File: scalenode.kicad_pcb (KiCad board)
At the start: 4 copper layers, 155.5 x 40 mm, 135 parts, among them IC1 TPS2378DDA, J1 B2B-XH-A_LF__SN_, J10 LSHM-130-01-L-RH-A-S-K-TR, J3 1-2199230-6, J4 1140084168, J5 0473460001, J6 SS-74800-144, J7 DF40HC(3.0)-100DS-0.4v, J8 DF40HC(3.0)-100DS-0.4v, M1 compute-module-4-1.5mm, Q6 BSS138-7-F, U1 TS3USB30EDGSR, U2 TPS62823DLCT, U5 TS3USB30EDGSR, U6 FT234XD-R

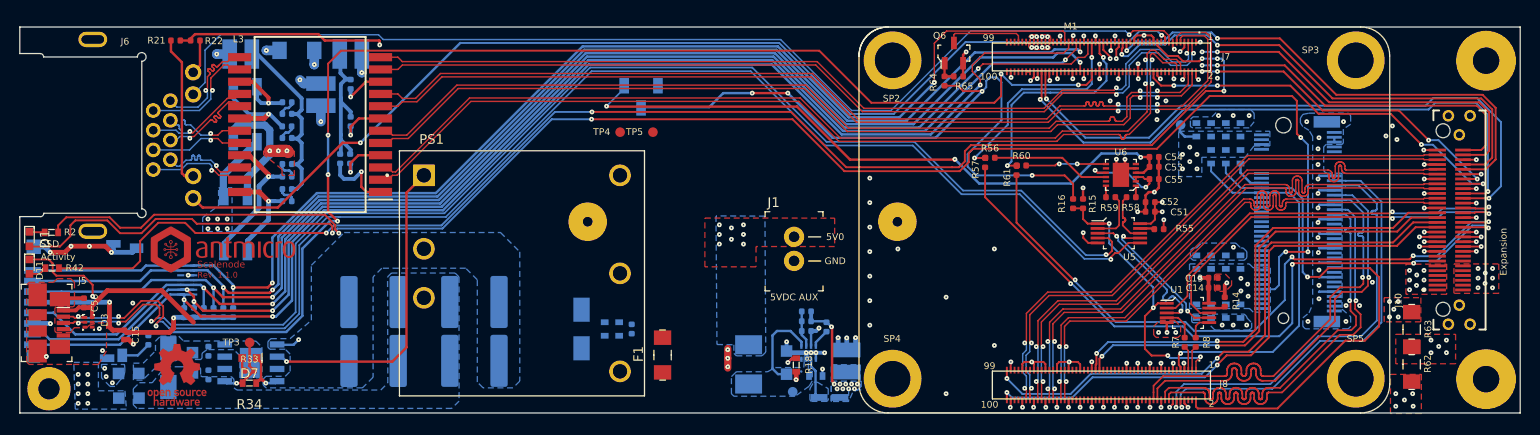
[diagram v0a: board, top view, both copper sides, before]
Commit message: Initial connection of all nets
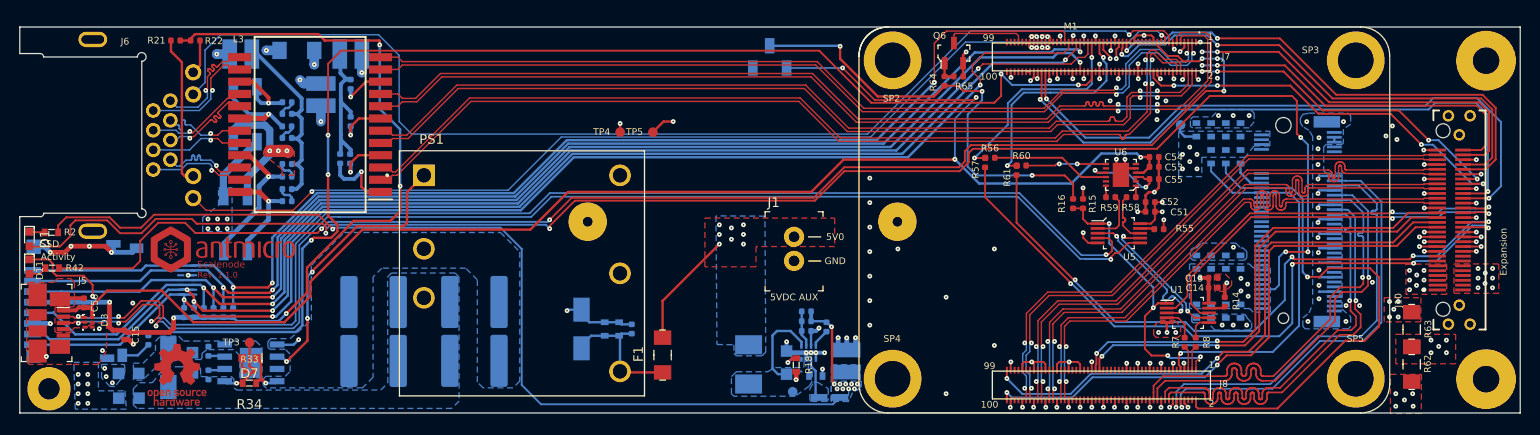
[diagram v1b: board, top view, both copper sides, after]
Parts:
- moved S1 14.0 mm to (132.8, 59.7), turned to 180 degrees
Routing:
- net /Interfaces/VBus_Slave: track 83.5 -> 157.4 mm, vias 3 -> 4
- net 3V3_SSD: track 44.3 -> 111.9 mm
- net 3V3_RPi: track 74.3 -> 116.1 mm, vias 16 -> 18
- net PROG_MODE: track 70.7 -> 47.3 mm, vias 4 -> 3
- net VCC5V0: track 0.00 -> 14.7 mm, vias 24 -> 25
- net Net-(C35-Pad1): track 0.00 -> 14.2 mm
- net /Interfaces/CONN_USB_P: track 140.5 -> 130.2 mm
- net /Interfaces/CONN_USB_N: track 142.0 -> 133.9 mm
- net ETH_LEDY: track 115.7 -> 109.1 mm
- net GND: track 157.3 -> 163.9 mm, vias 151 -> 150
- net SD_DAT3: track 132.8 -> 126.7 mm
- net SD_DAT2: track 134.1 -> 128.0 mm
- net SD_CMD: track 132.9 -> 126.8 mm
- net SD_DAT0: track 135.1 -> 129.0 mm
- net SD_CLK: track 136.5 -> 130.5 mm
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
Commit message: Shortened board. Adjusted posiitons of components. Routed all signals. Added stitching cap
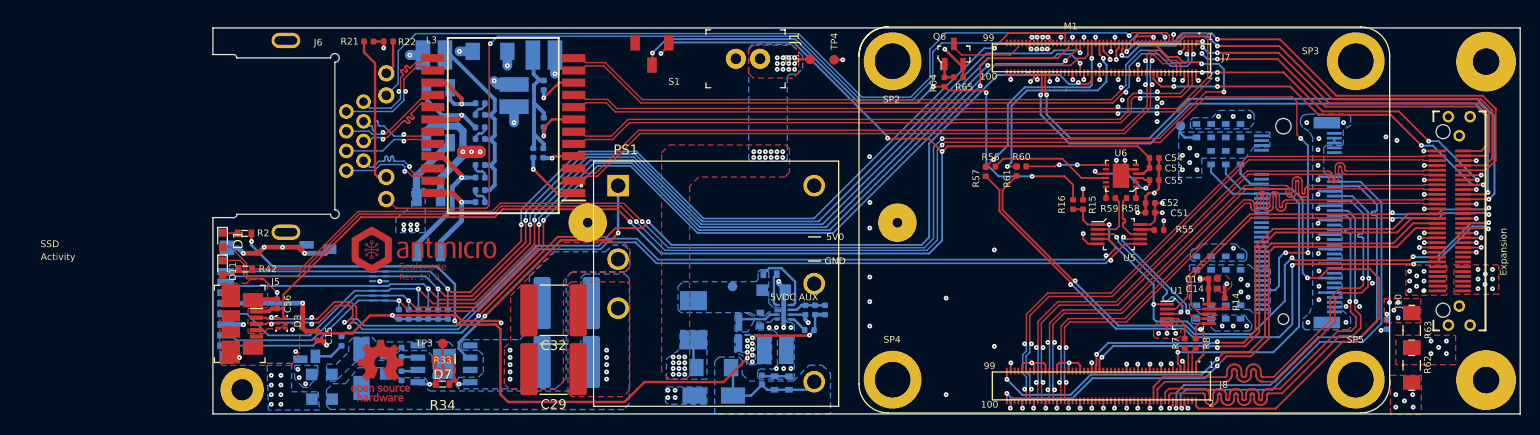
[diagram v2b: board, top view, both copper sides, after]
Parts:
- added C21: C_100n_0402, scalenode-footprints:0402-cap, B.Cu at (196.8, 87.4)
- C29, C32, S1: moved to F.Cu
- F1, R18: moved to B.Cu
- moved TP4 23.4 mm to (139.5, 60.0), turned to -90 degrees
- moved R11 22.3 mm to (97.4, 86.4)
- moved R12 22.3 mm to (98.4, 86.4)
- moved R9 22.3 mm to (95.4, 86.4)
- moved R10 22.3 mm to (96.4, 86.4)
- moved R13 22.3 mm to (99.5, 86.4)
- moved R5 22.3 mm to (94.4, 86.4)
- moved N3 21.1 mm to (92.5, 92.2)
- moved N1 20.8 mm to (97.4, 79.8)
- moved PS1 20.2 mm to (127.2, 83.2)
- moved R28 20.0 mm to (109.3, 69.7)
- moved R27 20.0 mm to (108.3, 69.7)
- moved C20 20.0 mm to (93.0, 91.5)
- moved C25 20.0 mm to (109.4, 59.5)
- moved C26 20.0 mm to (111.8, 85.2)
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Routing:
- net 3V3_RPi: track 116.1 -> 63.5 mm, vias 18 -> 16
- net GPIO3: track 132.7 -> 98.2 mm, vias 5 -> 3
- net 3V3_SSD: track 111.9 -> 80.1 mm, vias 25 -> 27
- net /Interfaces/CONN_USB_N: track 133.9 -> 103.5 mm
- net /Interfaces/CONN_USB_P: track 130.2 -> 102.5 mm
- net ETH_LEDG: track 119.5 -> 94.2 mm
- net TRD2_N: track 100.7 -> 75.6 mm
- net TRD1_N: track 93.1 -> 68.4 mm
- net TRD0_P: track 97.0 -> 72.6 mm
- net TRD1_P: track 93.1 -> 69.0 mm
- net TRD0_N: track 97.1 -> 73.3 mm
- net TRD2_P: track 100.7 -> 77.3 mm
- net TRD3_P: track 93.0 -> 72.1 mm
- net TRD3_N: track 92.5 -> 71.6 mm
- net SD_DAT1: track 130.8 -> 110.7 mm
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- added copper zone on F.Cu, net /PoE/VDD_POE_IN
- added copper zone on F.Cu, net GNDD
- added copper zone on B.Cu, net Net-(C35-Pad1)
- removed copper zone on F.Cu, net Net-(D4-Pad2)
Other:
- board size 155.5 x 40 mm -> 135.5 x 40 mm

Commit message: Optimized routes. Added missing 3D models
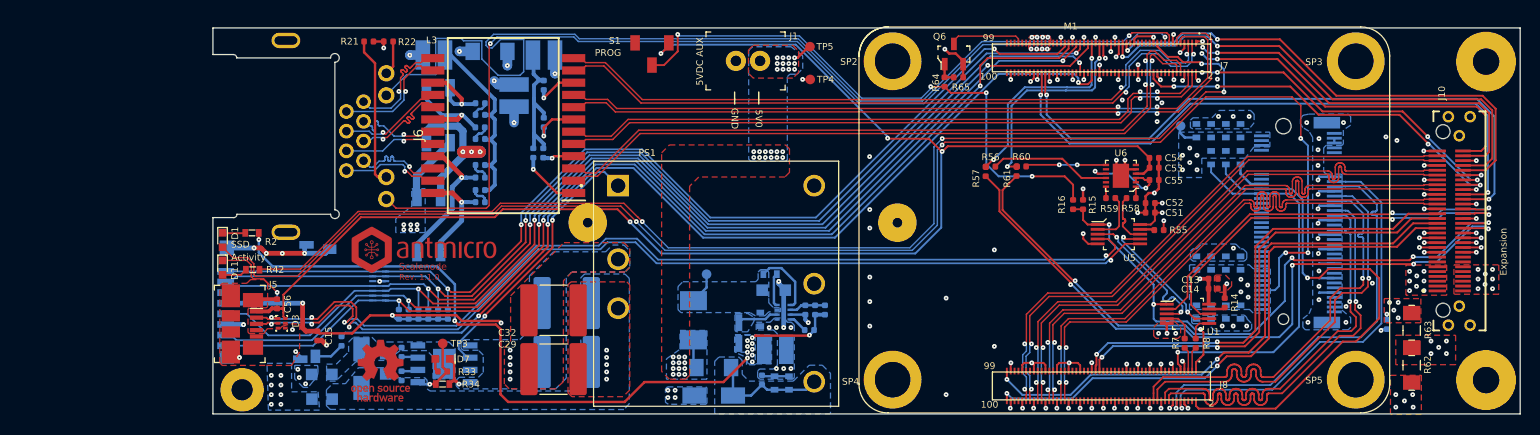
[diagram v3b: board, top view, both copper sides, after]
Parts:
- moved TP4 3.21 mm to (137.0, 62.0)
- moved TP1 2.98 mm to (126.3, 82.2)
- moved TP5 1.31 mm to (137.0, 58.6)
- moved R2 0.77 mm to (79.2, 77.9)
- moved R42 0.77 mm to (79.2, 81.8)
- moved J1 0.22 mm to (131.8, 60.1)
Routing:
- net ETH_LEDG: track 94.2 -> 106.8 mm
- net Net-(C16-Pad1): track 6.96 -> 10.3 mm
- net Net-(J7-Pad21): track 128.3 -> 126.7 mm
- net GND: track 154.0 -> 155.5 mm
- net ETH_LEDY: track 105.6 -> 104.2 mm
- net /Interfaces/VBus_Slave: track 150.4 -> 149.3 mm
- net RPi_RXD: track 22.6 -> 21.7 mm
- net Net-(J6-Pad12): track 3.59 -> 2.71 mm
- net Net-(D1-Pad2): track 154.6 -> 153.8 mm
- net SD_DAT2: track 109.9 -> 109.1 mm
- net Net-(D1-Pad1): track 1.87 -> 2.65 mm
- net Net-(D11-Pad2): track 2.18 -> 2.92 mm
- net SD_DAT1: track 110.7 -> 111.3 mm
- net GPIO26: track 41.4 -> 40.9 mm
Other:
- board text added: "Rev. ${REVISION}"
- board text removed: "Rev. 1.1.0"

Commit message: Corrected footprints. Adjusted position of testpoints. Cleared DRC
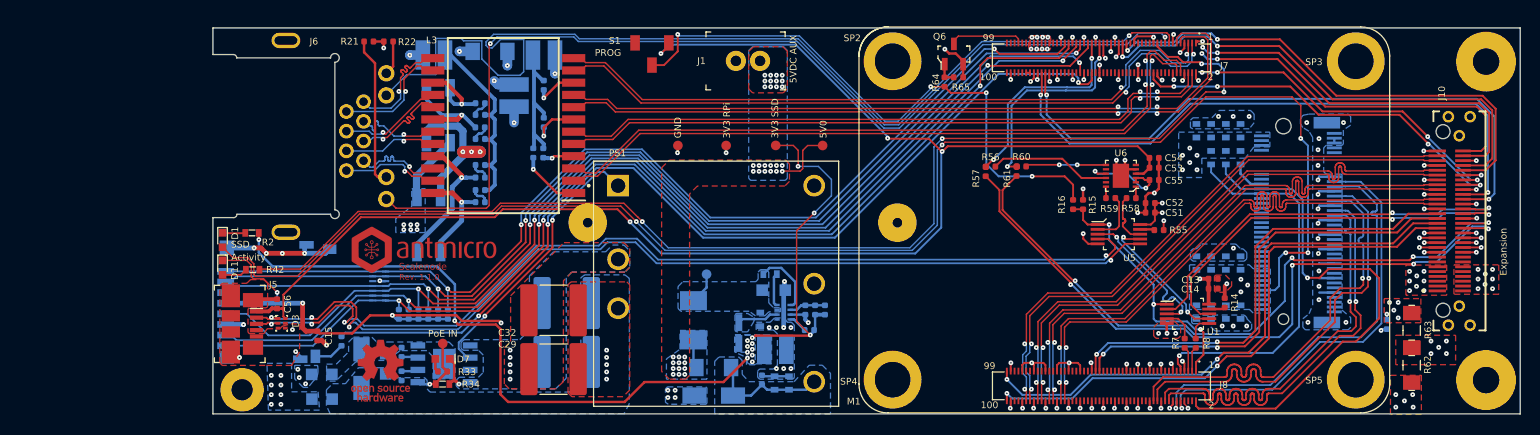
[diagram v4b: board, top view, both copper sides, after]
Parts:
- added TP6: TP_SMD1MM, scalenode-footprints:Testpoint_smd_1mm, F.Cu at (128.3, 68.9)
- TP2: moved to F.Cu
- moved TP2 42.0 mm to (133.5, 68.9), turned to 90 degrees
- moved TP4 15.3 mm to (123.3, 68.9), turned to 0 degrees
- moved TP5 10.3 mm to (138.3, 68.9)
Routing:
- net 3V3_SSD: track 79.9 -> 103.7 mm, vias 27 -> 29
- net VCC5V0: track 5.06 -> 9.39 mm
- net ETH_LEDG: track 106.8 -> 109.7 mm
- net ETH_LEDY: track 104.2 -> 106.3 mm
- net PROG_MODE: track 59.4 -> 61.4 mm
- net Net-(J6-Pad12): track 2.71 -> 3.59 mm
- net 3V3_RPi: track 63.5 -> 64.0 mm, vias 16 -> 17
- net GND: track 155.5 -> 155.2 mm, vias 149 -> 130
- net (no net): vias 1 -> 0
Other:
- board text added: "3V3 RPi"
- board text added: "3V3 SSD"
- board text added: "PoE IN"

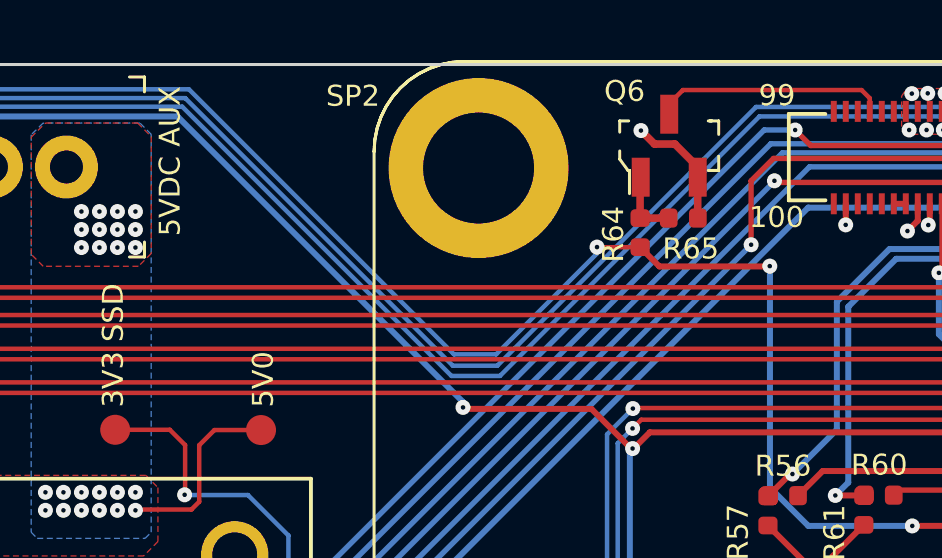
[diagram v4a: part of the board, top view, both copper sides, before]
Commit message: Added stackup table and defined stackup in board settings
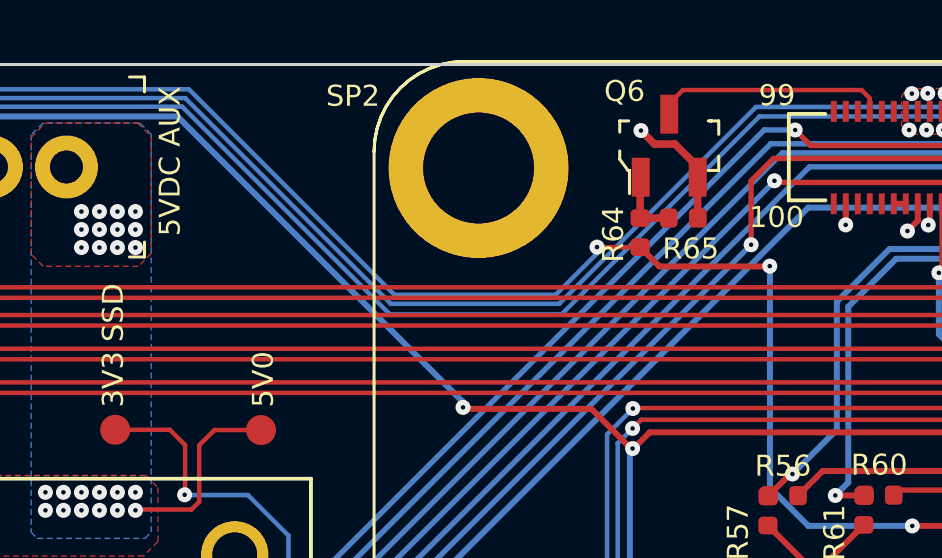
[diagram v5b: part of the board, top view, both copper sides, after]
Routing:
- net ETH_LEDG: track 109.7 -> 108.0 mm
- net ETH_LEDY: track 106.3 -> 104.6 mm
- net PROG_MODE: track 61.4 -> 59.8 mm
